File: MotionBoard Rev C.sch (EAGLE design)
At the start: 109 parts, among them IC1 LPC1769FBD100 or LPC4078FBD10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, IC2 LD1117, IC4 LMV324, Q1 NTGS3441T1G, Q2 12MHz, Q3 25MHz, U1 ARDUINO-FIREPICK+RAMPS, U2 101-00660-68-6, X2 USB-MICRO-B

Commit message: Update component values
Signed-off-by: Paul Jones <paul@pauljones.id.au>
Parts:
- removed PTC1: (no value), adafruit:PTCFUSE-1812
- R19, R20: value 49.9R -> 5R
- R58, R59, R60: value 33R -> 49.9R
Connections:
- removed net N$9: PTC1.2, X2.VCC
- net VUSB: now also X2.VCC; no longer PTC1.1
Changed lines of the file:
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@@
 <?xml version="1.0" encoding="utf-8"?>
 <!DOCTYPE eagle SYSTEM "eagle.dtd">
-<eagle version="7.3.0">
+<eagle version="7.5.0">
 <drawing>
 <settings>
@@
 <part name="SUPPLY18" library="supply2" deviceset="GND" device=""/>
 <part name="R53" library="resistor" deviceset="R-US_" device="R0603" value="10k"/>
-<part name="R58" library="resistor" deviceset="R-US_" device="R0603" value="33R"/>
-<part name="R59" library="resistor" deviceset="R-US_" device="R0603" value="33R"/>
-<part name="R60" library="resistor" deviceset="R-US_" device="R0603" value="33R"/>
+<part name="R58" library="resistor" deviceset="R-US_" device="R0603" value="49.9R"/>
+<part name="R59" library="resistor" deviceset="R-US_" device="R0603" value="49.9R"/>
+<part name="R60" library="resistor" deviceset="R-US_" device="R0603" value="49.9R"/>
 <part name="RJ1" library="Paul" deviceset="HR911105A" device=""/>
 <part name="SUPPLY19" library="supply2" deviceset="GND" device=""/>
@@
 <part name="SUPPLY6" library="supply2" deviceset="GND" device=""/>
 <part name="D1" library="SparkFun-DiscreteSemi" deviceset="DIODE" device="SOD123" value="MBR0530"/>
-<part name="PTC1" library="adafruit" deviceset="PTCFUSE" device="-1812"/>
 <part name="LED1" library="Paul" deviceset="LED" device=""/>
 <part name="LED2" library="Paul" deviceset="LED" device=""/>
@@
 <part name="SUPPLY32" library="supply2" deviceset="GND" device=""/>
 <part name="SUPPLY33" library="supply2" deviceset="GND" device=""/>
-<part name="R19" library="Paul" deviceset="RESISTOR" device="0603" value="49.9R"/>
+<part name="R19" library="Paul" deviceset="RESISTOR" device="0603" value="5R"/>
 <part name="C25" library="Paul" deviceset="CAP" device="0603" value="100n"/>
 <part name="SUPPLY35" library="supply2" deviceset="GND" device=""/>
@@
 <part name="SUPPLY37" library="SparkFun-Aesthetics" deviceset="5V" device=""/>
 <part name="L2" library="SparkFun" deviceset="INDUCTOR" device="0603" value="10uH"/>
-<part name="R20" library="Paul" deviceset="RESISTOR" device="0603" value="49.9R"/>
+<part name="R20" library="Paul" deviceset="RESISTOR" device="0603" value="5R"/>
 <part name="P+6" library="SparkFun" deviceset="3.3V" device=""/>
 </parts>
@@
 <attribute name="VALUE" x="20.5486" y="78.74" size="1.778" layer="96" rot="R270"/>
 </instance>
-<instance part="PTC1" gate="G$1" x="38.1" y="190.5" rot="R180"/>
 <instance part="LED1" gate="G$1" x="17.78" y="149.86" rot="R270"/>
 <instance part="LED2" gate="G$1" x="17.78" y="139.7" rot="R270"/>
@@
 </segment>
 <segment>
-<wire x1="43.18" y1="187.96" x2="48.26" y2="187.96" width="0.1524" layer="91"/>
 <label x="43.18" y="187.96" size="1.778" layer="95"/>
-<pinref part="PTC1" gate="G$1" pin="1"/>
+<wire x1="33.02" y1="182.88" x2="33.02" y2="187.96" width="0.1524" layer="91"/>
+<wire x1="27.94" y1="182.88" x2="33.02" y2="182.88" width="0.1524" layer="91"/>
+<pinref part="X2" gate="G$1" pin="VCC"/>
+<wire x1="48.26" y1="187.96" x2="33.02" y2="187.96" width="0.1524" layer="91"/>
 </segment>
 </net>
@@
 <pinref part="SUPPLY37" gate="G$1" pin="5V"/>
 <pinref part="L2" gate="G$1" pin="1"/>
-</segment>
-</net>
-<net name="N$9" class="0">
-<segment>
-<wire x1="33.02" y1="182.88" x2="33.02" y2="187.96" width="0.1524" layer="91"/>
-<pinref part="PTC1" gate="G$1" pin="2"/>
-<wire x1="27.94" y1="182.88" x2="33.02" y2="182.88" width="0.1524" layer="91"/>
-<pinref part="X2" gate="G$1" pin="VCC"/>
 </segment>
 </net>
@@
 <wire x1="226.06" y1="213.36" x2="226.06" y2="215.9" width="0.1524" layer="91"/>
 <pinref part="RJ1" gate="G$1" pin="GND"/>
-<wire x1="226.06" y1="215.9" x2="248.92" y2="215.9" width="0.1524" layer="91"/>
+<wire x1="226.06" y1="215.9" x2="250.19" y2="184.15" width="0.1524" layer="91"/>
 </segment>
 <segment>
@@
 <segment>
 <pinref part="RJ1" gate="G$1" pin="SHIELD1"/>
-<wire x1="248.92" y1="176.53" x2="241.3" y2="176.53" width="0.1524" layer="91"/>
+<wire x1="250.19" y1="176.53" x2="241.3" y2="176.53" width="0.1524" layer="91"/>
 <pinref part="SUPPLY62" gate="GND" pin="GND"/>
 <wire x1="241.3" y1="176.53" x2="241.3" y2="167.64" width="0.1524" layer="91"/>
 <pinref part="RJ1" gate="G$1" pin="SHIELD0"/>
-<wire x1="248.92" y1="179.07" x2="241.3" y2="179.07" width="0.1524" layer="91"/>
+<wire x1="250.19" y1="179.07" x2="241.3" y2="179.07" width="0.1524" layer="91"/>
 <wire x1="241.3" y1="179.07" x2="241.3" y2="176.53" width="0.1524" layer="91"/>
 <junction x="241.3" y="176.53"/>
@@
 <pinref part="IC8" gate="G$1" pin="TX+"/>
 <pinref part="RJ1" gate="G$1" pin="TD+"/>
-<wire x1="248.92" y1="198.12" x2="222.25" y2="198.12" width="0.1524" layer="91"/>
+<wire x1="250.19" y1="189.23" x2="222.25" y2="198.12" width="0.1524" layer="91"/>
 <pinref part="R54" gate="G$1" pin="2"/>
 <pinref part="C54" gate="G$1" pin="1"/>
@@
 <wire x1="147.32" y1="200.66" x2="177.8" y2="200.66" width="0.1524" layer="91"/>
 <wire x1="177.8" y1="200.66" x2="180.34" y2="200.66" width="0.1524" layer="91"/>
-<wire x1="248.92" y1="200.66" x2="180.34" y2="200.66" width="0.1524" layer="91"/>
+<wire x1="250.19" y1="199.39" x2="180.34" y2="200.66" width="0.1524" layer="91"/>
 <wire x1="180.34" y1="213.36" x2="180.34" y2="200.66" width="0.1524" layer="91"/>
 <junction x="180.34" y="200.66"/>
@@
 <pinref part="IC8" gate="G$1" pin="RX+"/>
 <pinref part="RJ1" gate="G$1" pin="RD+"/>
-<wire x1="248.92" y1="203.2" x2="231.14" y2="203.2" width="0.1524" layer="91"/>
+<wire x1="250.19" y1="201.93" x2="231.14" y2="203.2" width="0.1524" layer="91"/>
 <pinref part="R56" gate="G$1" pin="2"/>
 <pinref part="C56" gate="G$1" pin="1"/>
@@
 <wire x1="233.68" y1="172.72" x2="233.68" y2="210.82" width="0.1524" layer="91"/>
 <pinref part="RJ1" gate="G$1" pin="RD-"/>
-<wire x1="233.68" y1="210.82" x2="248.92" y2="210.82" width="0.1524" layer="91"/>
+<wire x1="233.68" y1="210.82" x2="250.19" y2="212.09" width="0.1524" layer="91"/>
 <pinref part="R57" gate="G$1" pin="2"/>
 <pinref part="C57" gate="G$1" pin="1"/>
@@
 <segment>
 <pinref part="RJ1" gate="G$1" pin="P4"/>
-<wire x1="248.92" y1="205.74" x2="241.3" y2="205.74" width="0.1524" layer="91"/>
+<wire x1="250.19" y1="194.31" x2="241.3" y2="205.74" width="0.1524" layer="91"/>
 <wire x1="241.3" y1="205.74" x2="241.3" y2="208.28" width="0.1524" layer="91"/>
 <pinref part="RJ1" gate="G$1" pin="P5"/>
-<wire x1="241.3" y1="208.28" x2="248.92" y2="208.28" width="0.1524" layer="91"/>
+<wire x1="241.3" y1="208.28" x2="250.19" y2="207.01" width="0.1524" layer="91"/>
 <wire x1="241.3" y1="208.28" x2="241.3" y2="233.68" width="0.1524" layer="91"/>
 <junction x="241.3" y="208.28"/>

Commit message: Forgot to update resistor divider values
Signed-off-by: Paul Jones <paul@pauljones.id.au>
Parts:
- R1, R15, R17, R3: value 170k -> 17k
- R16, R18, R2, R6: value 330k -> 33k
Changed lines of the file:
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@@
 <part name="SJ2" library="SparkFun-Passives" deviceset="JUMPER-PAD-2-NC_BY_TRACE" device="" value=""/>
 <part name="SJ3" library="SparkFun-Passives" deviceset="JUMPER-PAD-3-2OF3_NC_BY_TRACE" device="_SMALL" value=""/>
-<part name="R1" library="Paul" deviceset="RESISTOR" device="0603" value="170k"/>
-<part name="R2" library="Paul" deviceset="RESISTOR" device="0603" value="330k"/>
+<part name="R1" library="Paul" deviceset="RESISTOR" device="0603" value="17k"/>
+<part name="R2" library="Paul" deviceset="RESISTOR" device="0603" value="33k"/>
 <part name="JP1" library="pinhead-2" deviceset="PINHD-2X04" device="_2.54-SMD"/>
-<part name="R3" library="Paul" deviceset="RESISTOR" device="0603" value="170k"/>
-<part name="R6" library="Paul" deviceset="RESISTOR" device="0603" value="330k"/>
-<part name="R15" library="Paul" deviceset="RESISTOR" device="0603" value="170k"/>
-<part name="R16" library="Paul" deviceset="RESISTOR" device="0603" value="330k"/>
-<part name="R17" library="Paul" deviceset="RESISTOR" device="0603" value="170k"/>
-<part name="R18" library="Paul" deviceset="RESISTOR" device="0603" value="330k"/>
+<part name="R3" library="Paul" deviceset="RESISTOR" device="0603" value="17k"/>
+<part name="R6" library="Paul" deviceset="RESISTOR" device="0603" value="33k"/>
+<part name="R15" library="Paul" deviceset="RESISTOR" device="0603" value="17k"/>
+<part name="R16" library="Paul" deviceset="RESISTOR" device="0603" value="33k"/>
+<part name="R17" library="Paul" deviceset="RESISTOR" device="0603" value="17k"/>
+<part name="R18" library="Paul" deviceset="RESISTOR" device="0603" value="33k"/>
 <part name="C21" library="Paul" deviceset="CAP" device="0603" value="100n"/>
 <part name="C22" library="Paul" deviceset="CAP" device="0603" value="100n"/>

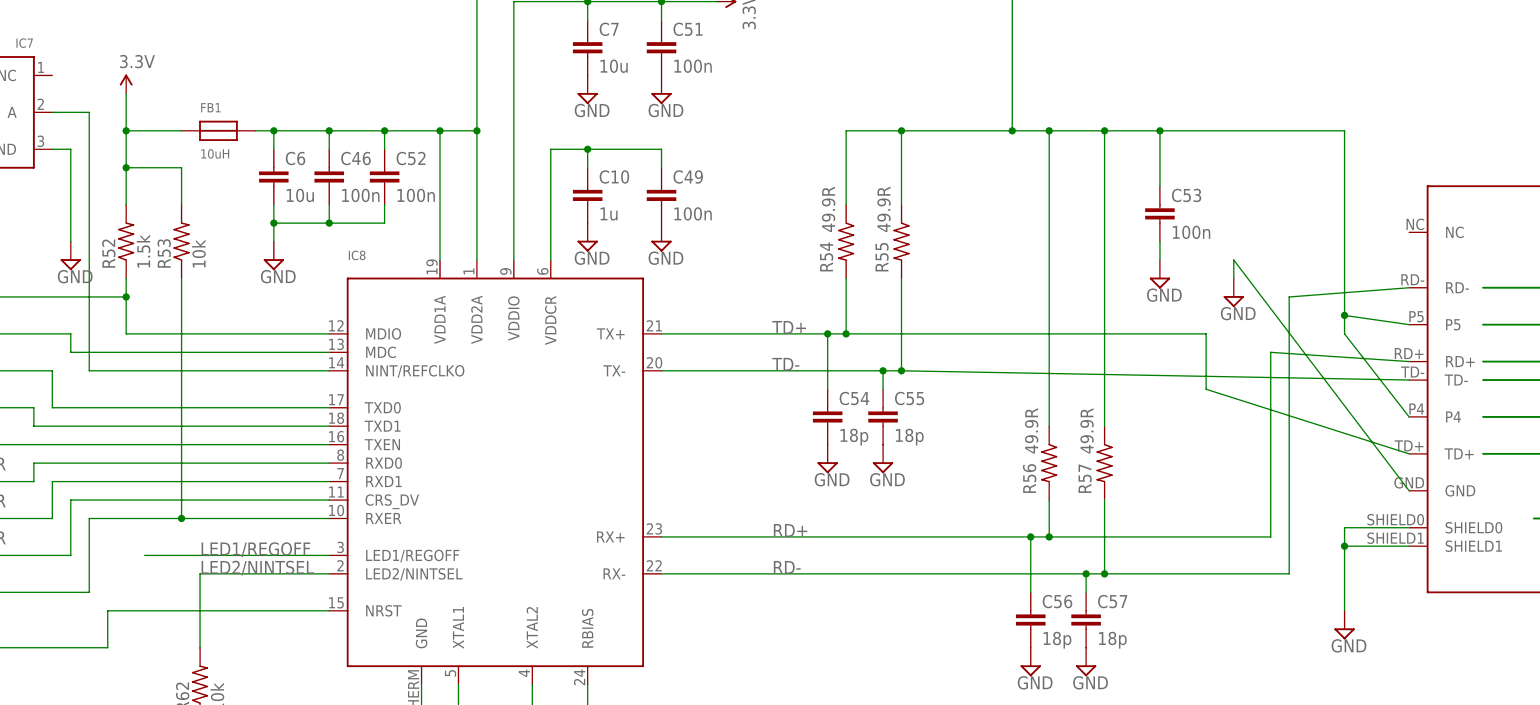
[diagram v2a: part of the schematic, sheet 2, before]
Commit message: Update component values
Signed-off-by: Paul Jones <paul@pauljones.id.au>
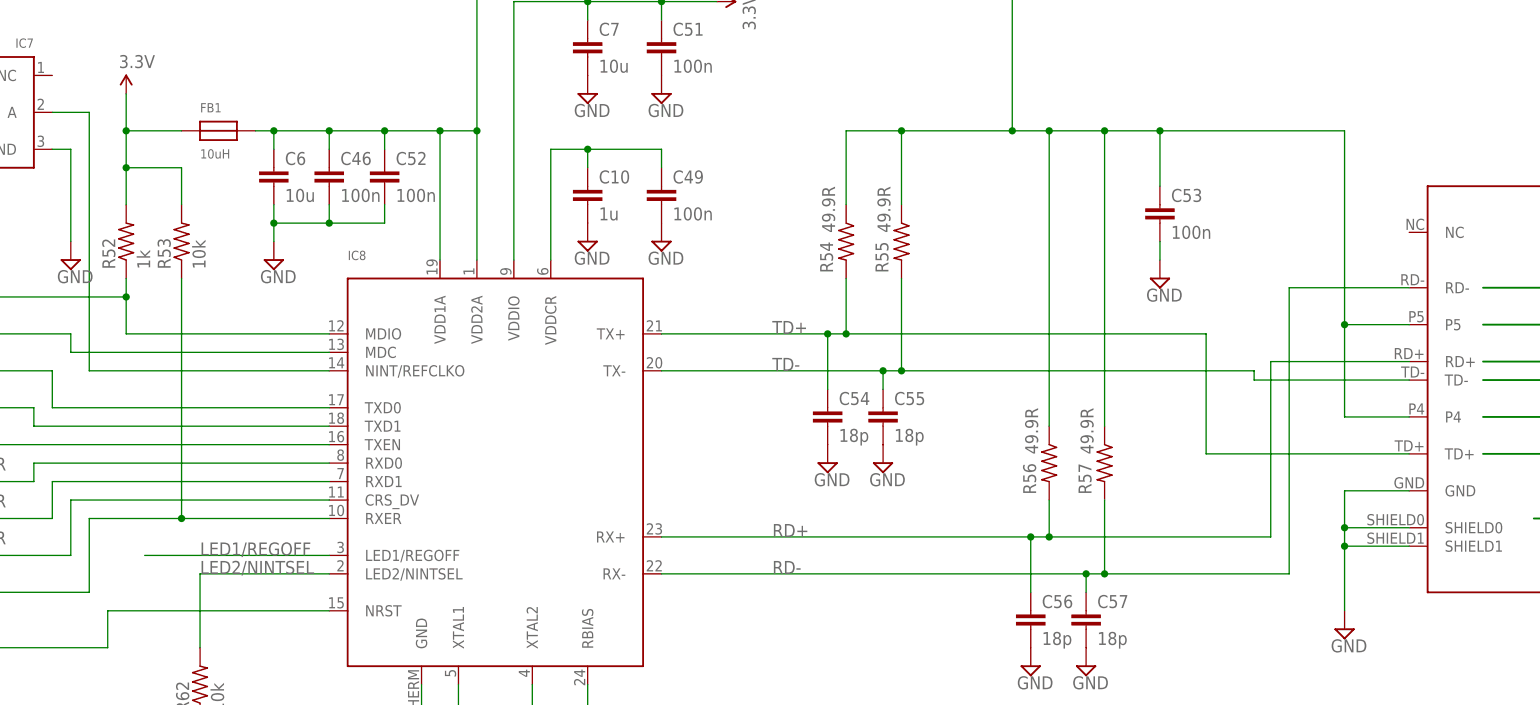
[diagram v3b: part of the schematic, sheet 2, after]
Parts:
- R52, R7: value 1.5k -> 1k
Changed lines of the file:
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@@
 <part name="P+16" library="SparkFun" deviceset="3.3V" device=""/>
 <part name="C14" library="Paul" deviceset="CAP" device="0603" value="100n"/>
-<part name="R7" library="resistor" deviceset="R-US_" device="R0603" value="1.5k"/>
+<part name="R7" library="resistor" deviceset="R-US_" device="R0603" value="1k"/>
 <part name="Q1" library="transistor-fet" deviceset="BSL207SP" device="" value="NTGS3441T1G"/>
 <part name="SUPPLY87" library="supply2" deviceset="GND" device=""/>
@@
 <part name="SUPPLY5" library="supply2" deviceset="GND" device=""/>
 <part name="IC8" library="microbuilder" deviceset="LAN8720" device=""/>
-<part name="R52" library="resistor" deviceset="R-US_" device="R0603" value="1.5k"/>
+<part name="R52" library="resistor" deviceset="R-US_" device="R0603" value="1k"/>
 <part name="R64" library="resistor" deviceset="R-US_" device="R0603" value="1M"/>
 <part name="R63" library="resistor" deviceset="R-US_" device="R0603" value="12.1k"/>
@@
 <part name="R60" library="resistor" deviceset="R-US_" device="R0603" value="49.9R"/>
 <part name="RJ1" library="Paul" deviceset="HR911105A" device=""/>
-<part name="SUPPLY19" library="supply2" deviceset="GND" device=""/>
 <part name="SUPPLY62" library="supply2" deviceset="GND" device=""/>
 <part name="SUPPLY70" library="supply2" deviceset="GND" device=""/>
@@
 </instance>
 <instance part="RJ1" gate="G$1" x="290.83" y="201.93"/>
-<instance part="SUPPLY19" gate="GND" x="226.06" y="210.82"/>
 <instance part="SUPPLY62" gate="GND" x="241.3" y="165.1"/>
 <instance part="SUPPLY70" gate="GND" x="325.12" y="157.48"/>
@@
 </segment>
 <segment>
-<pinref part="SUPPLY19" gate="GND" pin="GND"/>
-<wire x1="226.06" y1="213.36" x2="226.06" y2="215.9" width="0.1524" layer="91"/>
-<pinref part="RJ1" gate="G$1" pin="GND"/>
-<wire x1="226.06" y1="215.9" x2="250.19" y2="184.15" width="0.1524" layer="91"/>
-</segment>
-<segment>
 <pinref part="R61" gate="G$1" pin="1"/>
 <wire x1="320.04" y1="162.56" x2="325.12" y2="162.56" width="0.1524" layer="91"/>
@@
 <pinref part="RJ1" gate="G$1" pin="SHIELD0"/>
 <wire x1="250.19" y1="179.07" x2="241.3" y2="179.07" width="0.1524" layer="91"/>
-<wire x1="241.3" y1="179.07" x2="241.3" y2="176.53" width="0.1524" layer="91"/>
+<wire x1="241.3" y1="179.07" x2="241.3" y2="178.816" width="0.1524" layer="91"/>
 <junction x="241.3" y="176.53"/>
+<pinref part="RJ1" gate="G$1" pin="GND"/>
+<wire x1="241.3" y1="178.816" x2="241.3" y2="176.53" width="0.1524" layer="91"/>
+<wire x1="250.19" y1="184.15" x2="241.3" y2="184.15" width="0.1524" layer="91"/>
+<wire x1="241.3" y1="184.15" x2="241.3" y2="179.07" width="0.1524" layer="91"/>
+<junction x="241.3" y="179.07"/>
 </segment>
 <segment>
@@
 <wire x1="147.32" y1="205.74" x2="170.18" y2="205.74" width="0.1524" layer="91"/>
 <wire x1="170.18" y1="205.74" x2="172.72" y2="205.74" width="0.1524" layer="91"/>
-<wire x1="222.25" y1="198.12" x2="222.25" y2="205.74" width="0.1524" layer="91"/>
+<wire x1="222.25" y1="189.23" x2="222.25" y2="205.74" width="0.1524" layer="91"/>
 <wire x1="222.25" y1="205.74" x2="172.72" y2="205.74" width="0.1524" layer="91"/>
 <wire x1="172.72" y1="213.36" x2="172.72" y2="205.74" width="0.1524" layer="91"/>
@@
 <pinref part="IC8" gate="G$1" pin="TX+"/>
 <pinref part="RJ1" gate="G$1" pin="TD+"/>
-<wire x1="250.19" y1="189.23" x2="222.25" y2="198.12" width="0.1524" layer="91"/>
+<wire x1="250.19" y1="189.23" x2="222.25" y2="189.23" width="0.1524" layer="91"/>
 <pinref part="R54" gate="G$1" pin="2"/>
 <pinref part="C54" gate="G$1" pin="1"/>
@@
 <wire x1="147.32" y1="200.66" x2="177.8" y2="200.66" width="0.1524" layer="91"/>
 <wire x1="177.8" y1="200.66" x2="180.34" y2="200.66" width="0.1524" layer="91"/>
-<wire x1="250.19" y1="199.39" x2="180.34" y2="200.66" width="0.1524" layer="91"/>
 <wire x1="180.34" y1="213.36" x2="180.34" y2="200.66" width="0.1524" layer="91"/>
-<junction x="180.34" y="200.66"/>
 <label x="162.56" y="200.66" size="1.778" layer="95"/>
 <pinref part="IC8" gate="G$1" pin="TX-"/>
-<pinref part="RJ1" gate="G$1" pin="TD-"/>
 <pinref part="R55" gate="G$1" pin="2"/>
 <pinref part="C55" gate="G$1" pin="1"/>
 <wire x1="177.8" y1="198.12" x2="177.8" y2="200.66" width="0.1524" layer="91"/>
 <junction x="177.8" y="200.66"/>
+<pinref part="RJ1" gate="G$1" pin="TD-"/>
+<wire x1="250.19" y1="199.39" x2="228.854" y2="199.39" width="0.1524" layer="91"/>
+<wire x1="228.854" y1="199.39" x2="228.854" y2="200.66" width="0.1524" layer="91"/>
+<wire x1="228.854" y1="200.66" x2="180.34" y2="200.66" width="0.1524" layer="91"/>
+<junction x="180.34" y="200.66"/>
 </segment>
 </net>
@@
 <wire x1="147.32" y1="177.8" x2="198.12" y2="177.8" width="0.1524" layer="91"/>
 <wire x1="198.12" y1="177.8" x2="200.66" y2="177.8" width="0.1524" layer="91"/>
-<wire x1="231.14" y1="203.2" x2="231.14" y2="177.8" width="0.1524" layer="91"/>
+<wire x1="231.14" y1="201.93" x2="231.14" y2="177.8" width="0.1524" layer="91"/>
 <wire x1="231.14" y1="177.8" x2="200.66" y2="177.8" width="0.1524" layer="91"/>
 <wire x1="200.66" y1="182.88" x2="200.66" y2="177.8" width="0.1524" layer="91"/>
@@
 <pinref part="IC8" gate="G$1" pin="RX+"/>
 <pinref part="RJ1" gate="G$1" pin="RD+"/>
-<wire x1="250.19" y1="201.93" x2="231.14" y2="203.2" width="0.1524" layer="91"/>
+<wire x1="250.19" y1="201.93" x2="231.14" y2="201.93" width="0.1524" layer="91"/>
 <pinref part="R56" gate="G$1" pin="2"/>
 <pinref part="C56" gate="G$1" pin="1"/>
@@
 <label x="162.56" y="172.72" size="1.778" layer="95"/>
 <pinref part="IC8" gate="G$1" pin="RX-"/>
-<wire x1="233.68" y1="172.72" x2="233.68" y2="210.82" width="0.1524" layer="91"/>
+<wire x1="233.68" y1="172.72" x2="233.68" y2="212.09" width="0.1524" layer="91"/>
 <pinref part="RJ1" gate="G$1" pin="RD-"/>
-<wire x1="233.68" y1="210.82" x2="250.19" y2="212.09" width="0.1524" layer="91"/>
+<wire x1="233.68" y1="212.09" x2="250.19" y2="212.09" width="0.1524" layer="91"/>
 <pinref part="R57" gate="G$1" pin="2"/>
 <pinref part="C57" gate="G$1" pin="1"/>
@@
 <segment>
 <pinref part="RJ1" gate="G$1" pin="P4"/>
-<wire x1="250.19" y1="194.31" x2="241.3" y2="205.74" width="0.1524" layer="91"/>
-<wire x1="241.3" y1="205.74" x2="241.3" y2="208.28" width="0.1524" layer="91"/>
+<wire x1="250.19" y1="194.31" x2="241.3" y2="194.31" width="0.1524" layer="91"/>
+<wire x1="241.3" y1="194.31" x2="241.3" y2="207.01" width="0.1524" layer="91"/>
 <pinref part="RJ1" gate="G$1" pin="P5"/>
-<wire x1="241.3" y1="208.28" x2="250.19" y2="207.01" width="0.1524" layer="91"/>
-<wire x1="241.3" y1="208.28" x2="241.3" y2="233.68" width="0.1524" layer="91"/>
-<junction x="241.3" y="208.28"/>
+<wire x1="241.3" y1="207.01" x2="250.19" y2="207.01" width="0.1524" layer="91"/>
+<wire x1="241.3" y1="207.01" x2="241.3" y2="233.68" width="0.1524" layer="91"/>
+<junction x="241.3" y="207.01"/>
 <wire x1="208.28" y1="233.68" x2="200.66" y2="233.68" width="0.1524" layer="91"/>
 <wire x1="200.66" y1="233.68" x2="195.58" y2="233.68" width="0.1524" layer="91"/>
